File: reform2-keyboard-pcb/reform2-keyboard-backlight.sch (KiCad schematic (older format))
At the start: 93 parts, among them U2 TPS61185

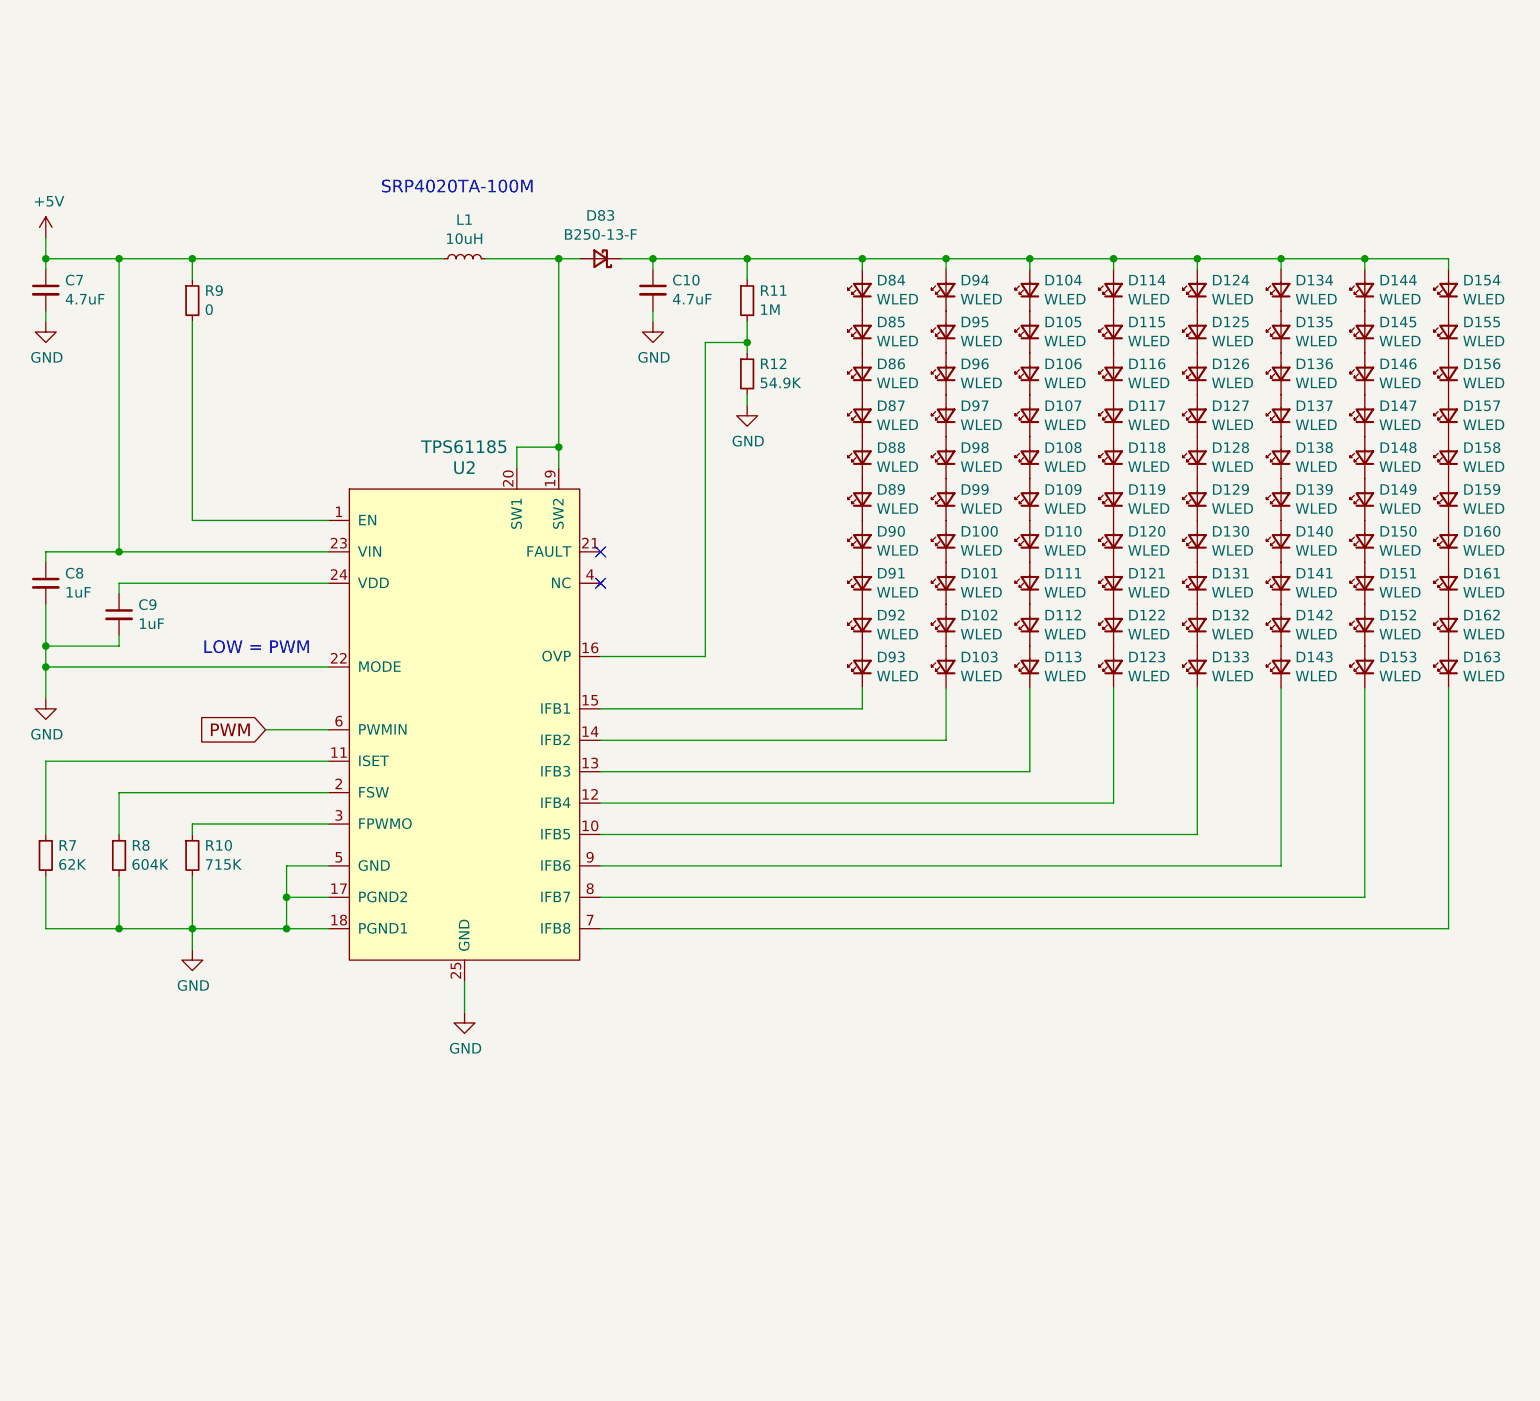
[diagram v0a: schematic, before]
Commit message: reform2: update PCBs incl. badges to production revs, add keyboard lettering, misc docs
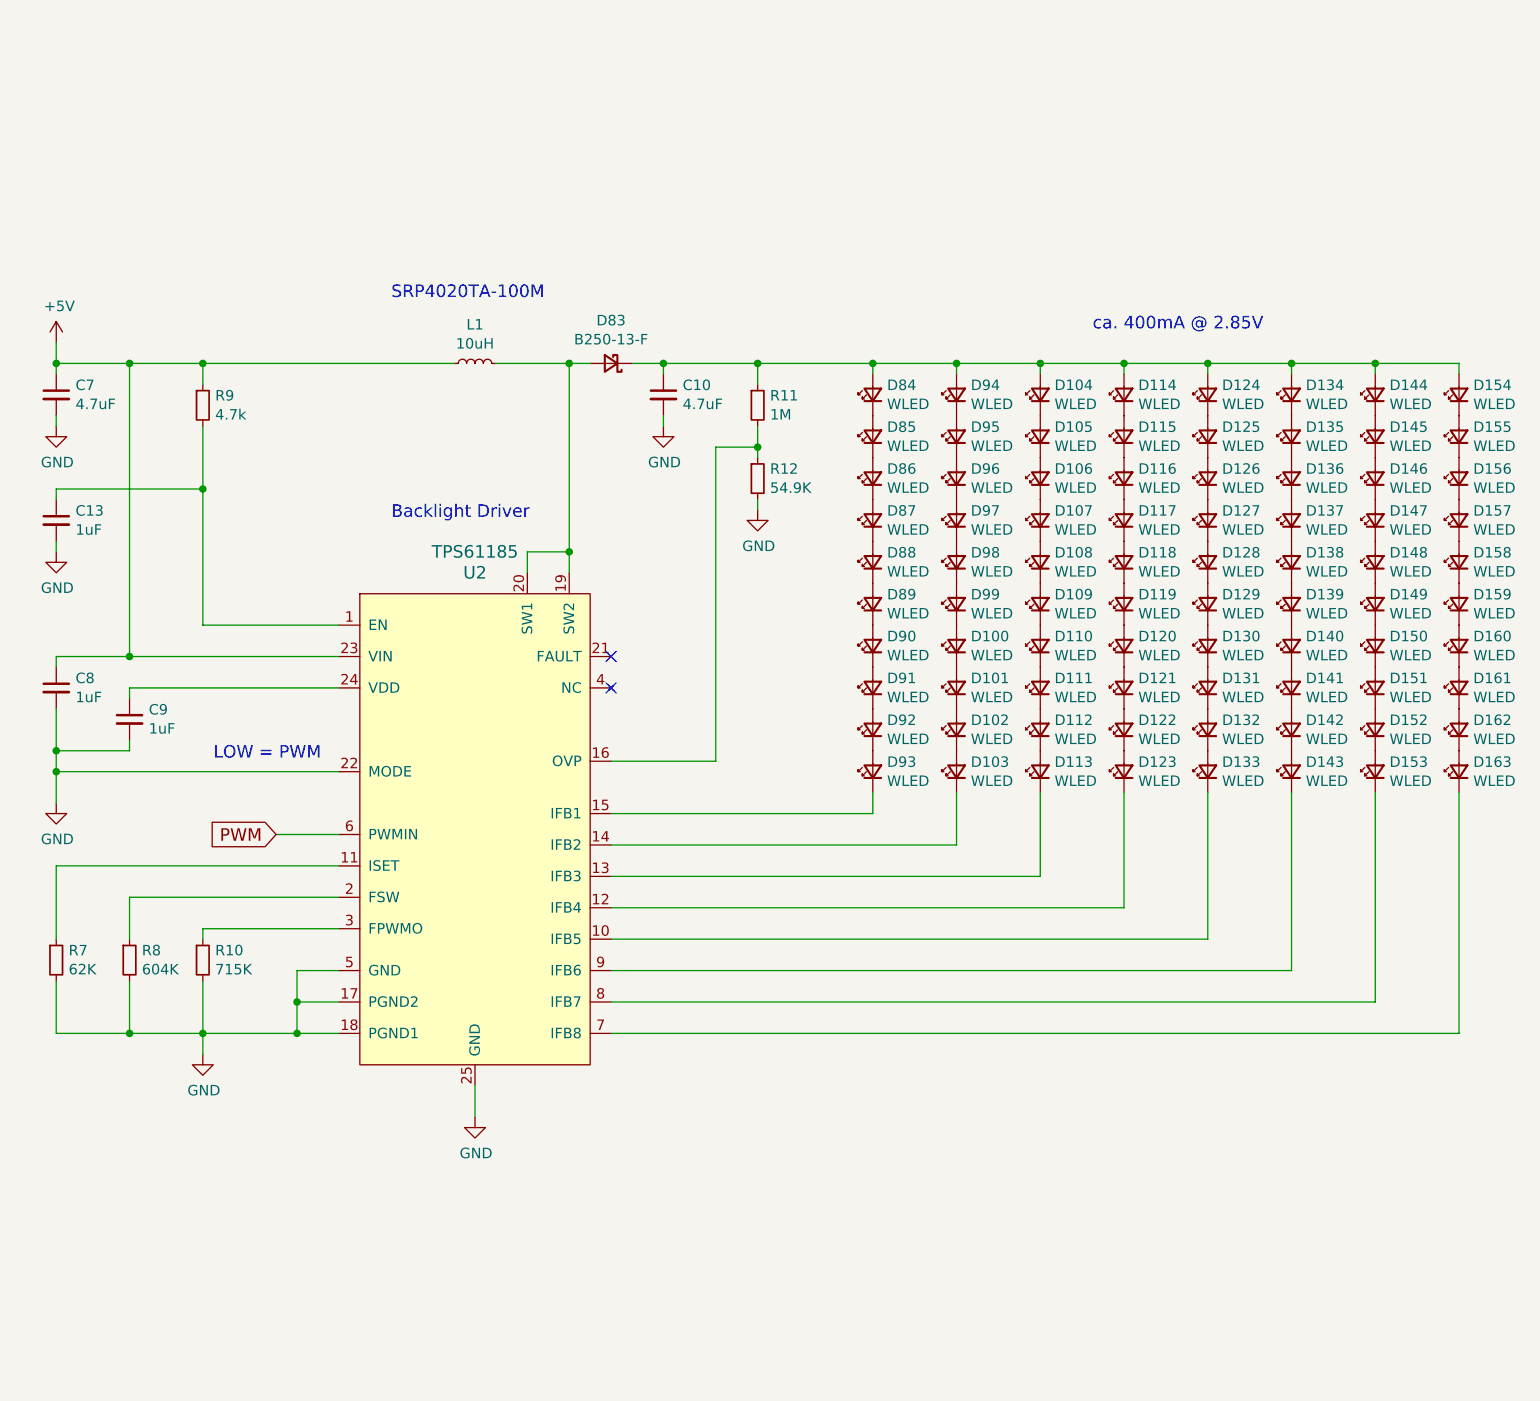
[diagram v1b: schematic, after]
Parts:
- added C13: 1uF, Capacitor_SMD:C_0603_1608Metric, symbol Device:C_Small
- R9: value 0 -> 4.7k; Manufacturer Vishay Dale -> Yageo; Manufacturer_No CRCW06030000Z0EAC -> RC0603FR-074K7L
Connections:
- net GND: now also C13.2
- net at R9.2, U2.1 (EN): now also C13.1
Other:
- note added: "Backlight Driver"
- note added: "ca. 400mA @ 2.85V"
- moved on the sheet: C10, C7, C8, C9, D100, D101, D102, D103, D104, D105, D106, D107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

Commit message: keyboard: add pcb version that has almost all components on the front side, with parts from lcsc
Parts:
- C10, C7: LCSC (none) -> C90057; Manufacturer Taiyo Yuden -> Murata; Manufacturer_No JMK107BB7475KA-T -> GRM188R61E475KE11D
- C13, C8, C9: LCSC (none) -> C14664; Manufacturer TDK -> Yageo; Manufacturer_No C1608X8L1C105K080AC -> CC0603KRX5R8BB105
- D100, D101, D102, D103, D104, D105, D106, D107, D108, D109, D110, D111, D112, D113, D114, D115, D116, D117, D118, D119, D120, D121, D122, D123, D124, D125, D126, D127, D128, D129, D130, D131, D132, D133, D134, D135, D136, D137, D138, D139, D140, D141, D142, D143, D144, D145, D146, D147, D148, D149, D150, D151, D152, D153, D154, D155, D156, D157, D158, D159, D160, D161, D162, D163, D84, D85, D86, D87, D88, D89, D90, D91, D92, D93, D94, D95, D96, D97, D98, D99: LCSC (none) -> C389521; Manufacturer OSRAM -> Meihua; Manufacturer_No LW Q38E-Q2OO-3K5L -> MHT192WDT-C2
- D83: Alt MPN (none) -> B250-13-F; Alt Manuf (none) -> Diodes; LCSC (none) -> C719400; Manufacturer Diodes -> UMW; Manufacturer_No B250-13-F -> SS26
- L1: Alt MPN (none) -> SRP4020TA-100M; Alt Manuf (none) -> Bourns; LCSC (none) -> C98364; Manufacturer Bourns -> Sunlord; Manufacturer_No SRP4020TA-100M -> WPN4020H100MT
- R10: LCSC (none) -> C137685; Manufacturer Vishay Dale -> Yageo; Manufacturer_No CRCW0603715KFKEA -> RC0603FR-07715KL
- R11: LCSC (none) -> C107698; Manufacturer_No RC0603FR-071ML -> RC0603JR-071ML
- R12: LCSC (none) -> C227961; Manufacturer_No RC0603FR-0754K9L -> AC0603FR-0754K9L
- R7: LCSC (none) -> C137694; Manufacturer Vishay Dale -> Yageo; Manufacturer_No CRCW060362K0FKEAC -> RC0603FR-0762KL
- R8: LCSC (none) -> C245986; Manufacturer Vishay Dale -> Yageo; Manufacturer_No CRCW0603604KFKEA -> RC0603FR-07604KL
- R9: LCSC (none) -> C105428; Manufacturer_No RC0603FR-074K7L -> RC0603JR-074K7L
- U2: LCSC (none) -> C2867853
